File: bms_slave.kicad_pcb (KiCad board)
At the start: 6 copper layers, 0 parts

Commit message: SCH: Schmatic is close to final, need to resolve a few ERC errors nothing major. Largest change will be adding seporate wires for VBAT and RefGround / Tap 0. connector position and types may change as mechaincal posision/layout is finalaized as well so holding off on layout for now.
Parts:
- added C1: 10nF, remote_cga3e3x7r1h474k080ae:C_0603_1608Metric, F.Cu at (224.0, 83.5)
- added C10: 0.47µF, remote_cga3e3x7r1h474k080ae:C_0603_1608Metric, F.Cu at (228.0, 91.0)
- added C11: 0.47µF, remote_cga3e3x7r1h474k080ae:C_0603_1608Metric, F.Cu at (228.0, 93.5)
- added C12: 0.47µF, remote_cga3e3x7r1h474k080ae:C_0603_1608Metric, F.Cu at (228.0, 96.1)
- added C13: 0.47µF, remote_cga3e3x7r1h474k080ae:C_0603_1608Metric, F.Cu at (232.0, 83.5)
- added C14: 0.47µF, remote_cga3e3x7r1h474k080ae:C_0603_1608Metric, F.Cu at (232.0, 86.0)
- added C15: 0.47µF, remote_cga3e3x7r1h474k080ae:C_0603_1608Metric, F.Cu at (232.0, 88.5)
- added C16: 0.47µF, remote_cga3e3x7r1h474k080ae:C_0603_1608Metric, F.Cu at (232.0, 91.0)
- added C17: 0.47µF, remote_cga3e3x7r1h474k080ae:C_0603_1608Metric, F.Cu at (232.0, 93.5)
- added C18: 0.47µF, remote_cga3e3x7r1h474k080ae:C_0603_1608Metric, F.Cu at (232.0, 96.1)
- added C19: 0.47µF, remote_cga3e3x7r1h474k080ae:C_0603_1608Metric, F.Cu at (236.0, 83.5)
- added C2: 0.47µF, remote_cga3e3x7r1h474k080ae:C_0603_1608Metric, F.Cu at (224.0, 86.0)
- added C20: 0.47µF, remote_cga3e3x7r1h474k080ae:C_0603_1608Metric, F.Cu at (236.0, 86.0)
- added C21: 2.2µF, remote_c0805x224k1racauto:C_0805_2012Metric, F.Cu at (136.1, 82.8)
- added C22: 1µF, remote_cga3e3x7r1h474k080ae:C_0603_1608Metric, F.Cu at (142.0, 93.2)
- added C23: 1µF, remote_cga3e3x7r1h474k080ae:C_0603_1608Metric, F.Cu at (223.6, 140.6)
- added C24: 4.7µF, remote_cl31b475kbhnfne:C_1206_3216Metric, F.Cu at (144.0, 87.2)
- added C25: 0.1µF, remote_cl05a105ko5nnnc:C_0402_1005Metric, F.Cu at (142.2, 88.8)
- added C26: 1µF, remote_cga3e3x7r1h474k080ae:C_0603_1608Metric, F.Cu at (223.6, 143.1)
- added C27: 0.1µF, remote_cl05a105ko5nnnc:C_0402_1005Metric, F.Cu at (228.7, 131.4)
- added C28: 0.22µF, remote_c0805x224k1racauto:C_0805_2012Metric, F.Cu at (227.8, 141.4)
- added C29: 0.1µF, remote_cl05a105ko5nnnc:C_0402_1005Metric, F.Cu at (275.4, 125.5)
- added C3: 0.47µF, remote_cga3e3x7r1h474k080ae:C_0603_1608Metric, F.Cu at (224.0, 88.5)
- added C30: 0.1µF, remote_cl05a105ko5nnnc:C_0402_1005Metric, F.Cu at (275.4, 127.5)
- added C31: 0.1µF, remote_cl05a105ko5nnnc:C_0402_1005Metric, F.Cu at (275.4, 129.5)
- added C32: 0.1µF, remote_cl05a105ko5nnnc:C_0402_1005Metric, F.Cu at (275.4, 131.4)
- added C33: 0.1µF, remote_cl05a105ko5nnnc:C_0402_1005Metric, F.Cu at (275.4, 133.4)
- added C34: 0.1µF, remote_cl05a105ko5nnnc:C_0402_1005Metric, F.Cu at (275.4, 135.4)
- added C35: 0.1µF, remote_cl05a105ko5nnnc:C_0402_1005Metric, F.Cu at (275.4, 137.3)
- added C36: 0.1µF, remote_cl05a105ko5nnnc:C_0402_1005Metric, F.Cu at (275.4, 139.3)
- added C37: 220pF, remote_cl05a105ko5nnnc:C_0402_1005Metric, F.Cu at (194.2, 47.5)
- added C38: 220pF, remote_cl05a105ko5nnnc:C_0402_1005Metric, F.Cu at (194.2, 49.5)
- added C39: 220pF, remote_cl05a105ko5nnnc:C_0402_1005Metric, F.Cu at (192.4, 140.4)
- added C4: 0.47µF, remote_cga3e3x7r1h474k080ae:C_0603_1608Metric, F.Cu at (224.0, 91.0)
- added C40: 220pF, remote_cl05a105ko5nnnc:C_0402_1005Metric, F.Cu at (192.4, 142.4)
- added C41: 100pF, remote_cl05a105ko5nnnc:C_0402_1005Metric, F.Cu at (194.2, 55.4)
- added C42: 100pF, remote_cl05a105ko5nnnc:C_0402_1005Metric, F.Cu at (192.4, 146.3)
- added C5: 0.47µF, remote_cga3e3x7r1h474k080ae:C_0603_1608Metric, F.Cu at (224.0, 93.5)
- added C6: 0.47µF, remote_cga3e3x7r1h474k080ae:C_0603_1608Metric, F.Cu at (224.0, 96.1)
- added C7: 0.47µF, remote_cga3e3x7r1h474k080ae:C_0603_1608Metric, F.Cu at (228.0, 83.5)
- added C8: 0.47µF, remote_cga3e3x7r1h474k080ae:C_0603_1608Metric, F.Cu at (228.0, 86.0)
- added C9: 0.47µF, remote_cga3e3x7r1h474k080ae:C_0603_1608Metric, F.Cu at (228.0, 88.5)
- added CR1: PESD1CAN,215, remote_pesd1can_215:SOT23_PESD1_NEX, F.Cu at (192.2, 60.9)
- added CR2: PESD1CAN,215, remote_pesd1can_215:SOT23_PESD1_NEX, F.Cu at (195.4, 149.9)
- added D1: Green, remote_ltst-c190tbkt:LED_0603_1608Metric, F.Cu at (227.9, 144.1)
- added D2: NSVR0340HT1G, remote_nsvr0340ht1g:SOD-323_1P7X1P25_ONS, F.Cu at (273.3, 141.9)
- added J1: 0436500200, remote_0436500200:CONN_SD-43650-001_02_MOL, F.Cu at (189.8, 82.2)
- added J2: 0430450200, remote_0430450200:CONN_SD-43045-001_02_MOL, F.Cu at (189.9, 100.7)
- added J3: 0436500900, remote_0436500900:CONN_SD-43650-001_09_MOL, F.Cu at (86.5, 65.8)
- added J4: 0430451600, remote_0430451600:CONN_SD-43045-001_16_MOL, F.Cu at (87.6, 100.8)
- added Q1: ZXTN4004KQTC, remote_zxtn4004kqtc:DPAK_04KQTC_DIO, F.Cu at (217.4, 134.2)
- added R1: 30, remote_rcs060359r0fkea:R_0603_1608Metric, F.Cu at (236.0, 88.5)
- added R10: 100, remote_rcs060359r0fkea:R_0603_1608Metric, F.Cu at (240.0, 86.0)
- added R11: 10, remote_crcw251210r0fkeg:R_2512_6332Metric, F.Cu at (217.6, 104.3)
- added R12: 100, remote_rcs060359r0fkea:R_0603_1608Metric, F.Cu at (240.0, 88.5)
- added R13: 10, remote_crcw251210r0fkeg:R_2512_6332Metric, F.Cu at (217.6, 109.3)
- added R14: 100, remote_rcs060359r0fkea:R_0603_1608Metric, F.Cu at (240.0, 91.0)
- added R15: 10, remote_crcw251210r0fkeg:R_2512_6332Metric, F.Cu at (217.6, 114.2)
- added R16: 100, remote_rcs060359r0fkea:R_0603_1608Metric, F.Cu at (240.0, 93.5)
- added R17: 10, remote_crcw251210r0fkeg:R_2512_6332Metric, F.Cu at (217.6, 119.1)
- added R18: 100, remote_rcs060359r0fkea:R_0603_1608Metric, F.Cu at (240.0, 96.1)
- added R19: 10, remote_crcw251210r0fkeg:R_2512_6332Metric, F.Cu at (217.6, 124.0)
- added R2: 100, remote_rcs060359r0fkea:R_0603_1608Metric, F.Cu at (236.0, 91.0)
- added R20: 150, remote_crcw1210150rfkea:R_1210_3225Metric, F.Cu at (224.4, 130.5)
- added R21: 150, remote_crcw1210150rfkea:R_1210_3225Metric, F.Cu at (224.4, 134.8)
- added R22: 2k, remote_erj-2ge0r00x:R_0402_1005Metric, F.Cu at (228.7, 133.4)
- added R23: 3.3k, remote_rcs060359r0fkea:R_0603_1608Metric, F.Cu at (269.0, 125.8)
- added R24: 3.3k, remote_rcs060359r0fkea:R_0603_1608Metric, F.Cu at (269.0, 128.3)
- added R25: 3.3k, remote_rcs060359r0fkea:R_0603_1608Metric, F.Cu at (269.0, 130.8)
- added R26: 3.3k, remote_rcs060359r0fkea:R_0603_1608Metric, F.Cu at (269.0, 133.3)
- added R27: 3.3k, remote_rcs060359r0fkea:R_0603_1608Metric, F.Cu at (269.0, 135.8)
- added R28: 3.3k, remote_rcs060359r0fkea:R_0603_1608Metric, F.Cu at (269.0, 138.3)
- added R29: 3.3k, remote_rcs060359r0fkea:R_0603_1608Metric, F.Cu at (269.0, 140.8)
- added R3: 10, remote_crcw251210r0fkeg:R_2512_6332Metric, F.Cu at (217.6, 84.7)
- added R30: 3.3k, remote_rcs060359r0fkea:R_0603_1608Metric, F.Cu at (269.0, 143.4)
- added R31: 10k, remote_erj-2ge0r00x:R_0402_1005Metric, F.Cu at (272.5, 125.5)
- added R32: 10k, remote_erj-2ge0r00x:R_0402_1005Metric, F.Cu at (272.5, 127.5)
- added R33: 10k, remote_erj-2ge0r00x:R_0402_1005Metric, F.Cu at (272.5, 129.5)
- added R34: 10k, remote_erj-2ge0r00x:R_0402_1005Metric, F.Cu at (272.5, 131.5)
- added R35: 10k, remote_erj-2ge0r00x:R_0402_1005Metric, F.Cu at (272.5, 133.5)
- added R36: 10k, remote_erj-2ge0r00x:R_0402_1005Metric, F.Cu at (272.5, 135.5)
- added R37: 10k, remote_erj-2ge0r00x:R_0402_1005Metric, F.Cu at (272.5, 137.5)
- added R38: 10k, remote_erj-2ge0r00x:R_0402_1005Metric, F.Cu at (272.5, 139.5)
- added R39: 1k, remote_erj-2ge0r00x:R_0402_1005Metric, F.Cu at (191.3, 47.5)
- added R4: 100, remote_rcs060359r0fkea:R_0603_1608Metric, F.Cu at (236.0, 93.5)
- added R40: 1k, remote_erj-2ge0r00x:R_0402_1005Metric, F.Cu at (189.5, 138.5)
- added R41: 49.9, remote_erj-2ge0r00x:R_0402_1005Metric, F.Cu at (191.3, 51.5)
- added R42: 49.9, remote_erj-2ge0r00x:R_0402_1005Metric, F.Cu at (191.3, 53.5)
- added R43: 49.9, remote_erj-2ge0r00x:R_0402_1005Metric, F.Cu at (189.5, 144.5)
- added R44: 49.9, remote_erj-2ge0r00x:R_0402_1005Metric, F.Cu at (189.5, 146.5)
- added R5: 10, remote_crcw251210r0fkeg:R_2512_6332Metric, F.Cu at (217.6, 89.6)
- added R6: 100, remote_rcs060359r0fkea:R_0603_1608Metric, F.Cu at (236.0, 96.1)
- added R7: 10, remote_crcw251210r0fkeg:R_2512_6332Metric, F.Cu at (217.6, 94.5)
- added R8: 100, remote_rcs060359r0fkea:R_0603_1608Metric, F.Cu at (240.0, 83.5)
- added R9: 10, remote_crcw251210r0fkeg:R_2512_6332Metric, F.Cu at (217.6, 99.4)
- added TP1: ~, TestPoint:TestPoint_Pad_D2.0mm, F.Cu at (95.0, 143.1)
- added TP10: ~, TestPoint:TestPoint_Pad_D2.0mm, F.Cu at (95.0, 137.0)
- added TP11: ~, TestPoint:TestPoint_Pad_D2.0mm, F.Cu at (89.0, 132.9)
- added TP12: ~, TestPoint:TestPoint_Pad_D2.0mm, F.Cu at (89.0, 137.0)
- added TP13: ~, TestPoint:TestPoint_Pad_D2.0mm, F.Cu at (89.0, 141.1)
- added TP14: ~, TestPoint:TestPoint_Pad_D2.0mm, F.Cu at (89.0, 145.1)
- added TP2: ~, TestPoint:TestPoint_Pad_D2.0mm, F.Cu at (95.0, 147.1)
- added TP3: ~, TestPoint:TestPoint_Pad_D2.0mm, F.Cu at (99.0, 143.1)
- added TP4: ~, TestPoint:TestPoint_Pad_D2.0mm, F.Cu at (99.0, 147.1)
- added TP5: ~, TestPoint:TestPoint_Pad_D2.0mm, F.Cu at (103.1, 143.1)
- added TP6: ~, TestPoint:TestPoint_Pad_D2.0mm, F.Cu at (103.1, 147.1)
- added TP7: ~, TestPoint:TestPoint_Pad_D2.0mm, F.Cu at (107.2, 143.1)
- added TP8: ~, TestPoint:TestPoint_Pad_D2.0mm, F.Cu at (107.2, 147.1)
- added TP9: ~, TestPoint:TestPoint_Pad_D2.0mm, F.Cu at (95.0, 132.9)
- added U1: BQ79616PAPRQ1, remote_bq79616paprq1:BQ79616PAPRQ1, F.Cu at (132.7, 91.0)
- added U2: SM91502ALA-E, remote_sm91502ala-e:IC6_SM91502ALA-E_BRN, F.Cu at (174.2, 51.0)
- added U3: SM91502ALA-E, remote_sm91502ala-e:IC6_SM91502ALA-E_BRN, F.Cu at (179.8, 144.8)
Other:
- board outline added: 101 x 38 mm
- copper layers 6 -> 4
- rule pad_to_mask_clearance: 0.05 -> 0

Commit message: SCH[Cleaning]:Updated Connectors not sure still, added sprate bat and ground connections, updated commincation conncetors. PCB[Layout]:Inital layout of compents need to fit on board size once tap connecton method is decided.
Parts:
- removed the J4 at (87.6, 100.8)
- added FID1: Fiducial, Fiducial:Fiducial_0.5mm_Mask1mm, F.Cu at (110.5, 130.7)
- added FID2: Fiducial, Fiducial:Fiducial_0.5mm_Mask1mm, F.Cu at (110.5, 133.2)
- added FID3: Fiducial, Fiducial:Fiducial_0.5mm_Mask1mm, F.Cu at (110.5, 135.8)
- added H1: MountingHole, MountingHole:MountingHole_3.2mm_M3, F.Cu at (103.8, 106.2)
- added H2: MountingHole, MountingHole:MountingHole_3.2mm_M3, F.Cu at (171.2, 106.2)
- added H3: MountingHole, MountingHole:MountingHole_3.2mm_M3, F.Cu at (171.2, 68.8)
- added H4: MountingHole, MountingHole:MountingHole_3.2mm_M3, F.Cu at (103.8, 68.8)
- added J4: 0436501200, remote_0436501200:CONN_SD-43650-001_12_MOL, F.Cu at (68.8, 101.0)
- added J4: 0430451200, remote_0430451200:CONN_SD-43045-001_12_MOL, F.Cu at (24.8, 137.1)
- J1: value 0436500200 -> 0436500218; footprint remote_0436500200:CONN_SD-43650-001_02_MOL -> remote_0436500218:CONN_SD-43650-007_02_MOL
- J2: value 0430450200 -> 0430450212; footprint remote_0430450200:CONN_SD-43045-001_02_MOL -> remote_0430450212:CONN_SD-43045-005_02_MOL
- J3: value 0436500900 -> 0430451612; footprint remote_0436500900:CONN_SD-43650-001_09_MOL -> remote_0430451612:CONN_SD-43045-005_16_MOL
- moved R18 165.1 mm to (78.0, 64.0)
- moved R16 163.8 mm to (78.0, 69.5)
- moved R14 163.0 mm to (77.8, 75.0)
- moved R12 162.4 mm to (77.8, 79.5)
- moved R8 162.3 mm to (77.8, 89.5)
- moved R10 162.2 mm to (77.8, 85.0)
- moved R1 162.2 mm to (75.0, 108.0)
- moved C29 161.3 mm to (121.5, 77.0), turned to 180 degrees
- moved R2 159.4 mm to (77.0, 103.0)
- moved R4 159.1 mm to (77.0, 100.0)
- moved R6 159.0 mm to (77.0, 94.5)
- moved R31 158.6 mm to (122.0, 75.5), turned to -90 degrees
- moved C30 157.0 mm to (126.7, 77.0)
- moved C31 155.7 mm to (128.7, 77.1), turned to 180 degrees
- moved R32 155.3 mm to (126.1, 75.5), turned to -90 degrees
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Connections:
- C37 pad 1: /Project Architecture/Daisy Chain/U1_COMLP -> /Project Architecture/Daisy Chain/U1_COMLN
- C38 pad 1: /Project Architecture/Daisy Chain/U1_COMLN -> /Project Architecture/Daisy Chain/U1_COMLP
- CR1 pad 2: /Project Architecture/Daisy Chain/COML_WN -> /Project Architecture/Daisy Chain/COML_WP
- J1 pad 1: /Project Architecture/Connectors/COML.P -> /Project Architecture/Connectors/COML.N
- J1 pad 2: /Project Architecture/Connectors/COML.N -> /Project Architecture/Connectors/COML.P
- J3 pad 1: /Project Architecture/Cell Sense & Balance/TAP0 -> /Project Architecture/Connectors/T_P8
- J3 pad 2: /Project Architecture/Cell Sense & Balance/TAP1 -> /Project Architecture/Connectors/T_P7
- J3 pad 3: /Project Architecture/Cell Sense & Balance/TAP2 -> /Project Architecture/Connectors/T_P6
- J3 pad 4: /Project Architecture/Cell Sense & Balance/TAP3 -> /Project Architecture/Connectors/T_P5
- J3 pad 5: /Project Architecture/Cell Sense & Balance/TAP4 -> /Project Architecture/Connectors/T_P4
- J3 pad 6: /Project Architecture/Cell Sense & Balance/TAP5 -> /Project Architecture/Connectors/T_P3
- J3 pad 7: /Project Architecture/Cell Sense & Balance/TAP6 -> /Project Architecture/Connectors/T_P2
- J3 pad 8: /Project Architecture/Cell Sense & Balance/TAP7 -> /Project Architecture/Connectors/T_P1
- J3 pad 9: /Project Architecture/Cell Sense & Balance/TAP8 -> /Project Architecture/GND
- R1 pad 1: /Project Architecture/Cell Sense & Balance/TAP8 -> /Project Architecture/VMODULE
- R20 pad 1: /Project Architecture/Cell Sense & Balance/VMODULE -> /Project Architecture/VMODULE
- R39 pad 1: /Project Architecture/Daisy Chain/U1_COMLP -> /Project Architecture/Daisy Chain/U1_COMLN
- R39 pad 2: /Project Architecture/Daisy Chain/U1_COMLN -> /Project Architecture/Daisy Chain/U1_COMLP
- R41 pad 1: /Project Architecture/Daisy Chain/U1_COMLP -> /Project Architecture/Daisy Chain/U1_COMLN
- R42 pad 1: /Project Architecture/Daisy Chain/U1_COMLN -> /Project Architecture/Daisy Chain/U1_COMLP
- R42 pad 2: /Project Architecture/Daisy Chain/COML_WN -> /Project Architecture/Daisy Chain/COML_WP
- U2 pad 3: /Project Architecture/Daisy Chain/COML_WN -> /Project Architecture/Daisy Chain/COML_WP
- U2 pad 4: /Project Architecture/Connectors/COML.N -> /Project Architecture/Connectors/COML.P
- U2 pad 6: /Project Architecture/Connectors/COML.P -> /Project Architecture/Connectors/COML.N
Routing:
- net /Project Architecture/Daisy Chain/COML_WP: track 0.00 -> 15.7 mm
- net /Project Architecture/Daisy Chain/COMH_WP: track 0.00 -> 7.80 mm
- net /Project Architecture/Daisy Chain/COMH_WN: track 0.00 -> 7.80 mm
- net /Project Architecture/Connectors/COML.N: track 0.00 -> 7.11 mm
- net /Project Architecture/Connectors/COMH.P: track 0.00 -> 6.92 mm
- net /Project Architecture/Connectors/COML.P: track 0.00 -> 6.92 mm
- net /Project Architecture/Connectors/COMH.N: track 0.00 -> 6.87 mm
- net /Project Architecture/Daisy Chain/U1_COMLN: track 0.00 -> 2.39 mm
- net /Project Architecture/Daisy Chain/U1_COMHN: track 0.00 -> 2.16 mm
- net /Project Architecture/Daisy Chain/U1_COMHP: track 0.00 -> 2.08 mm
- net /Project Architecture/Daisy Chain/U1_COMLP: track 0.00 -> 2.07 mm
- net /Project Architecture/Daisy Chain/COML_CT: track 0.00 -> 1.42 mm
- net /Project Architecture/Daisy Chain/COMH_CT: track 0.00 -> 1.37 mm
- added copper zone on F.Cu, net /Project Architecture/GND
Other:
- board size 101 x 38 mm -> 75 x 45 mm

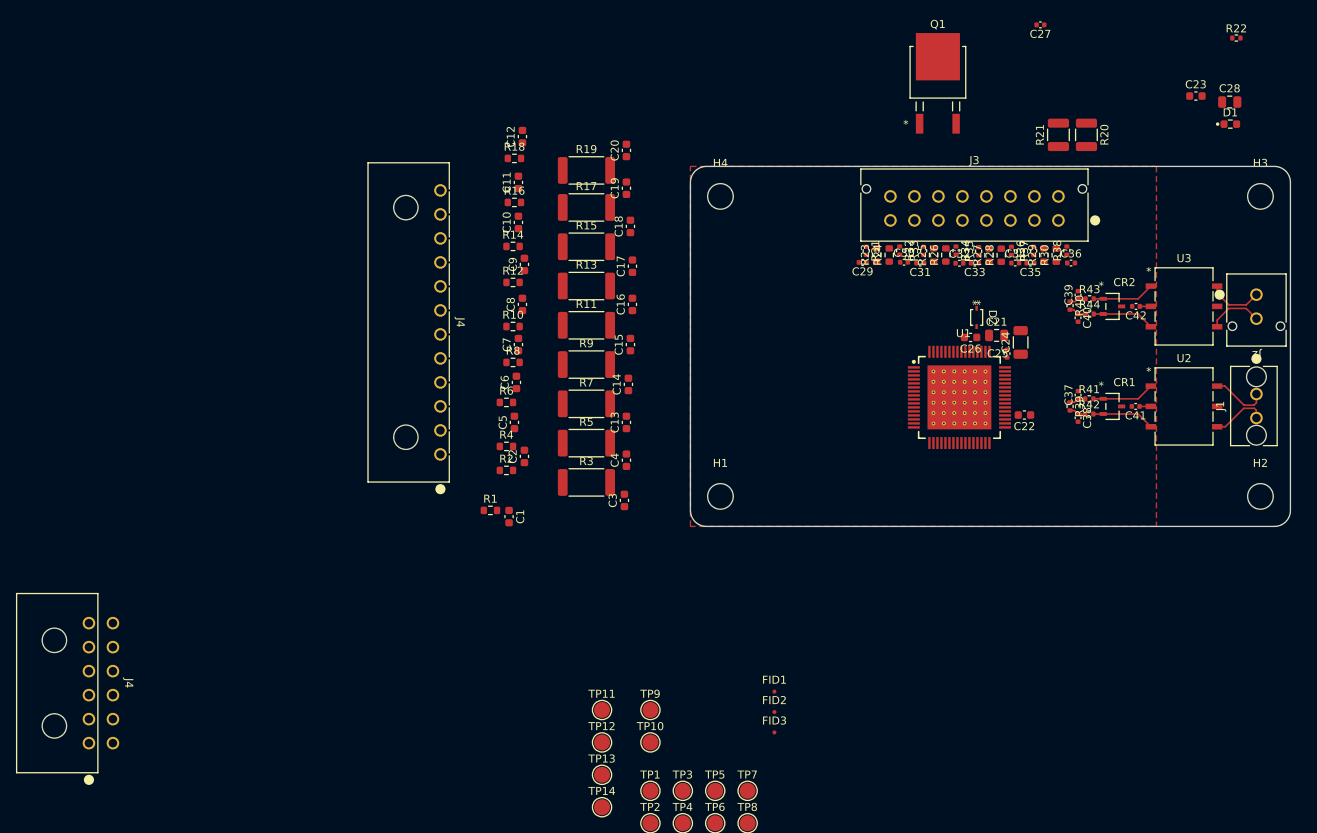
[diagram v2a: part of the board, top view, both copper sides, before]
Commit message: PCB[Part Layout]: Working on routing and part arragement more, thinking im going to go with the two row connector for bat connections, might have to put parts on both sides for cleaner routing for bal/sens filter caps. 0603 so wouldnt be too bad to solder.
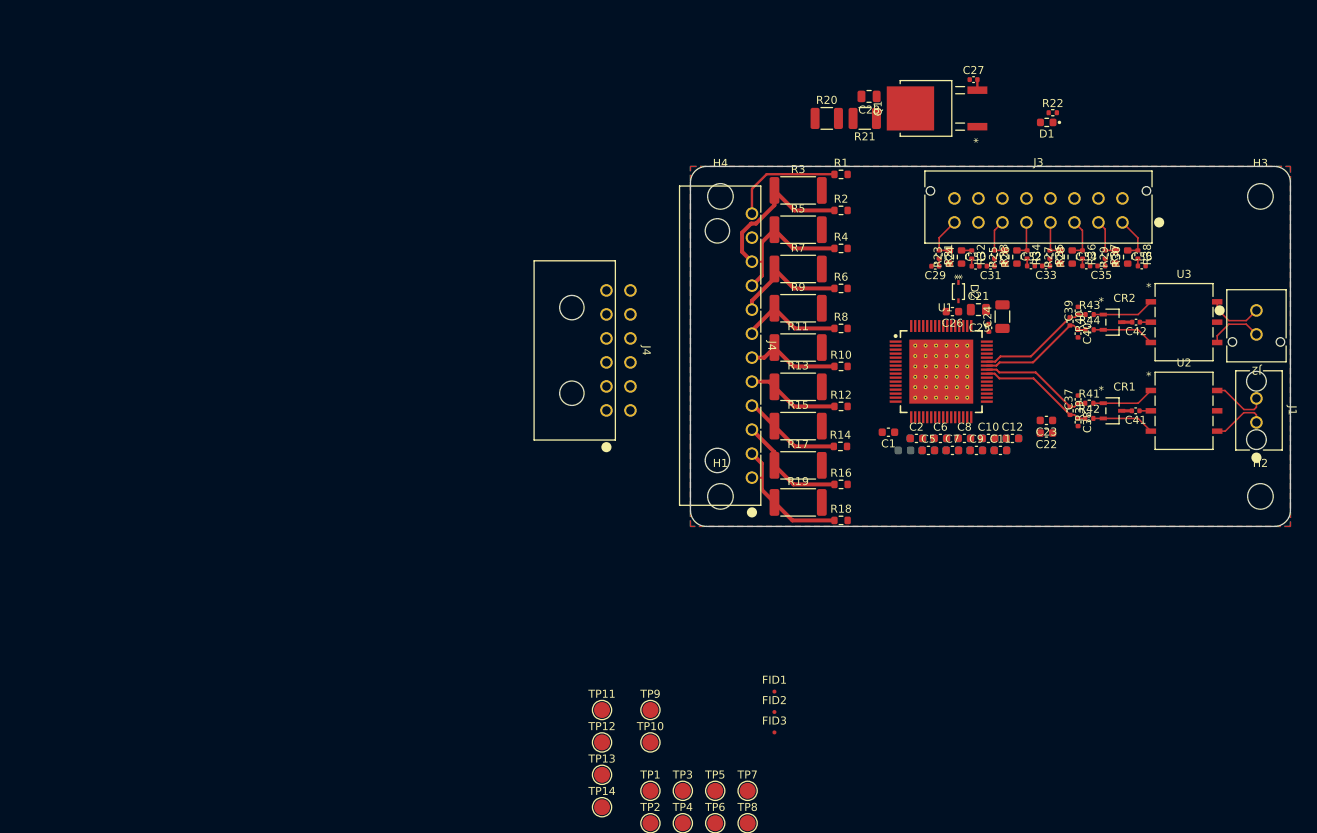
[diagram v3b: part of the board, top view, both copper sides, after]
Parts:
- C13, C14, C15, C16, C17, C18, C19, C20, C3, C4: moved to B.Cu
- moved J4 76.9 mm to (89.5, 95.5)
- moved C12 71.9 mm to (140.2, 99.0), turned to 0 degrees
- moved C11 68.9 mm to (138.8, 100.5), turned to 0 degrees
- moved C10 64.7 mm to (137.2, 99.0), turned to 0 degrees
- moved C9 61.1 mm to (135.8, 100.5), turned to 0 degrees
- moved R18 60.9 mm to (118.8, 109.2)
- moved R1 60.7 mm to (118.8, 66.0)
- moved C20 60.2 mm to (140.2, 99.0), turned to 0 degrees
- moved C8 57.7 mm to (134.2, 99.0), turned to 0 degrees
- moved C19 57.1 mm to (138.8, 100.5), turned to 0 degrees
- moved C7 55.8 mm to (132.8, 100.5), turned to 0 degrees
- moved R16 53.9 mm to (118.8, 104.8)
- moved C6 53.5 mm to (131.2, 99.0), turned to 0 degrees
- moved R2 53.0 mm to (118.8, 70.5)
- moved C18 52.0 mm to (137.3, 99.0), turned to 0 degrees
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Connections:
- J1 pad 1: /Project Architecture/Connectors/COML.N -> /Project Architecture/Connectors/COML.P
- J1 pad 2: /Project Architecture/Connectors/COML.P -> /Project Architecture/Connectors/COML.N
- J4 pad 1: /Project Architecture/VMODULE -> /Project Architecture/GND
- J4 pad 10: /Project Architecture/Cell Sense & Balance/TAP1 -> /Project Architecture/Cell Sense & Balance/TAP8
- J4 pad 11: /Project Architecture/Cell Sense & Balance/TAP0 -> unconnected-(J4-Pad11)
- J4 pad 12: /Project Architecture/GND -> /Project Architecture/VMODULE
- J4 pad 2: unconnected-(J4-Pad2) -> /Project Architecture/Cell Sense & Balance/TAP0
- J4 pad 3: /Project Architecture/Cell Sense & Balance/TAP8 -> /Project Architecture/Cell Sense & Balance/TAP1
- J4 pad 4: /Project Architecture/Cell Sense & Balance/TAP7 -> /Project Architecture/Cell Sense & Balance/TAP2
- J4 pad 5: /Project Architecture/Cell Sense & Balance/TAP6 -> /Project Architecture/Cell Sense & Balance/TAP3
- J4 pad 6: /Project Architecture/Cell Sense & Balance/TAP5 -> /Project Architecture/Cell Sense & Balance/TAP4
- J4 pad 7: /Project Architecture/Cell Sense & Balance/TAP4 -> /Project Architecture/Cell Sense & Balance/TAP5
- J4 pad 8: /Project Architecture/Cell Sense & Balance/TAP3 -> /Project Architecture/Cell Sense & Balance/TAP6
- J4 pad 9: /Project Architecture/Cell Sense & Balance/TAP2 -> /Project Architecture/Cell Sense & Balance/TAP7
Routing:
- net /Project Architecture/Cell Sense & Balance/TAP8: track 0.00 -> 20.0 mm
- net /Project Architecture/Cell Sense & Balance/TAP7: track 0.00 -> 16.6 mm
- net /Project Architecture/Cell Sense & Balance/TAP0: track 0.00 -> 15.7 mm
- net /Project Architecture/Cell Sense & Balance/TAP6: track 0.00 -> 14.8 mm
- net /Project Architecture/VMODULE: track 0.00 -> 14.2 mm
- net /Project Architecture/Cell Sense & Balance/TAP1: track 0.00 -> 14.1 mm
- net /Project Architecture/Cell Sense & Balance/TAP5: track 0.00 -> 12.9 mm
- net /Project Architecture/Daisy Chain/U1_COMHP: track 2.08 -> 14.8 mm
- net /Project Architecture/Daisy Chain/U1_COMLP: track 2.07 -> 14.6 mm
- net /Project Architecture/Daisy Chain/U1_COMHN: track 2.16 -> 14.6 mm
- net /Project Architecture/Cell Sense & Balance/TAP2: track 0.00 -> 12.3 mm
- net /Project Architecture/Daisy Chain/U1_COMLN: track 2.39 -> 14.4 mm
- net /Project Architecture/Cell Sense & Balance/TAP4: track 0.00 -> 11.8 mm
- net /Project Architecture/Cell Sense & Balance/TAP3: track 0.00 -> 11.6 mm
- net /Project Architecture/Connectors/T_P8: track 0.00 -> 5.57 mm
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- added copper zone on B.Cu, net /Project Architecture/GND
- added copper zone on In1.Cu, net /Project Architecture/GND
- added copper zone on In2.Cu, net /Project Architecture/GND

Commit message: PCB[Rules]: Updated rules, via & trace size, clearnace, and board stackup.
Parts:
- moved J4 31.5 mm to (76.2, 102.3)
- moved C25 8.03 mm to (144.0, 80.8)
- moved C23 7.70 mm to (150.4, 101.7)
- moved C22 7.69 mm to (150.1, 103.6)
- moved U1 4.73 mm to (136.0, 90.1)
- moved J4 4.32 mm to (93.8, 95.3)
- moved C24 3.91 mm to (141.8, 81.0)
- moved C21 3.83 mm to (138.5, 80.0)
- moved C1 3.70 mm to (128.4, 98.8)
- moved C12 3.58 mm to (143.8, 98.8)
- moved C11 3.53 mm to (142.3, 100.3)
- moved C10 3.48 mm to (140.7, 98.8)
- moved C9 3.43 mm to (139.2, 100.3)
- moved C8 3.38 mm to (137.6, 98.8)
- moved C7 3.33 mm to (136.1, 100.3)
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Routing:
- net /Project Architecture/Cell Sense & Balance/VC8: track 0.00 -> 46.6 mm
- net /Project Architecture/Cell Sense & Balance/VC7: track 0.00 -> 43.3 mm
- net /Project Architecture/Cell Sense & Balance/VC6: track 0.00 -> 40.6 mm
- net /Project Architecture/Cell Sense & Balance/VC0: track 0.00 -> 36.1 mm
- net /Project Architecture/Cell Sense & Balance/VC5: track 0.00 -> 34.9 mm
- net /Project Architecture/Cell Sense & Balance/VC4: track 0.00 -> 32.7 mm
- net /Project Architecture/Cell Sense & Balance/VC1: track 0.00 -> 32.5 mm
- net /Project Architecture/Cell Sense & Balance/VC3: track 0.00 -> 30.7 mm
- net /Project Architecture/Cell Sense & Balance/VC2: track 0.00 -> 28.4 mm
- net /Project Architecture/Cell Sense & Balance/TAP0: track 15.7 -> 0.00 mm
- net /Project Architecture/VMODULE: track 14.2 -> 0.00 mm
- net /Project Architecture/Cell Sense & Balance/TAP8: track 20.0 -> 8.42 mm
- net /Project Architecture/Cell Sense & Balance/TAP7: track 16.6 -> 8.42 mm
- net /Project Architecture/Cell Sense & Balance/TAP1: track 14.1 -> 8.42 mm
- net /Project Architecture/Cell Sense & Balance/TAP6: track 14.8 -> 9.58 mm
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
